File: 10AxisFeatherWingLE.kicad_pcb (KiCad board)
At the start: 2 copper layers, 50.8 x 22.9 mm, 23 parts, among them J1 feather long, J2 feather short, J3 feather long, J4 feather short, J5 feather breakout, J6 stemma connector, U1 LSM9DS1, U2 BMP280

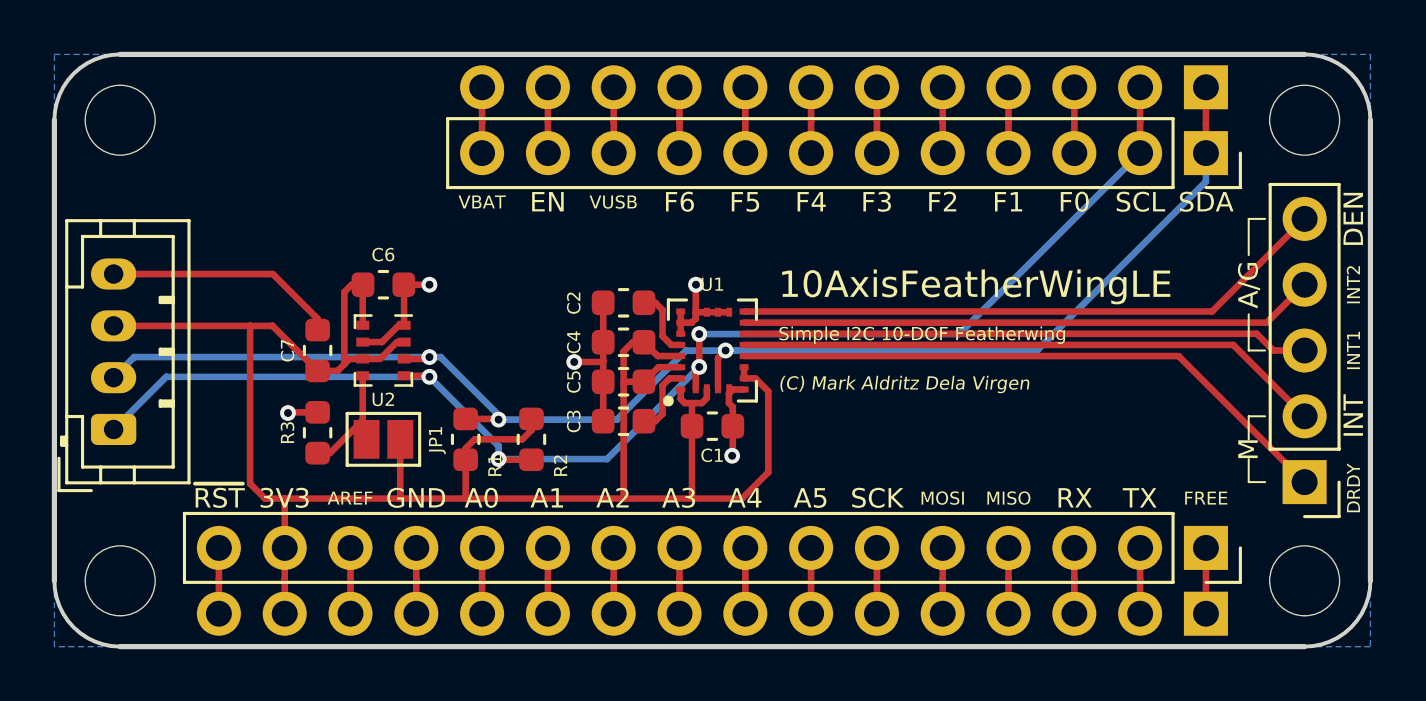
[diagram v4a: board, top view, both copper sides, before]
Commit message: Removed STEMMA connector
STEMMA requires the use of a 3.3V to 5V level shifter and voltage regulator.
The board does not support these features, so they were removed.
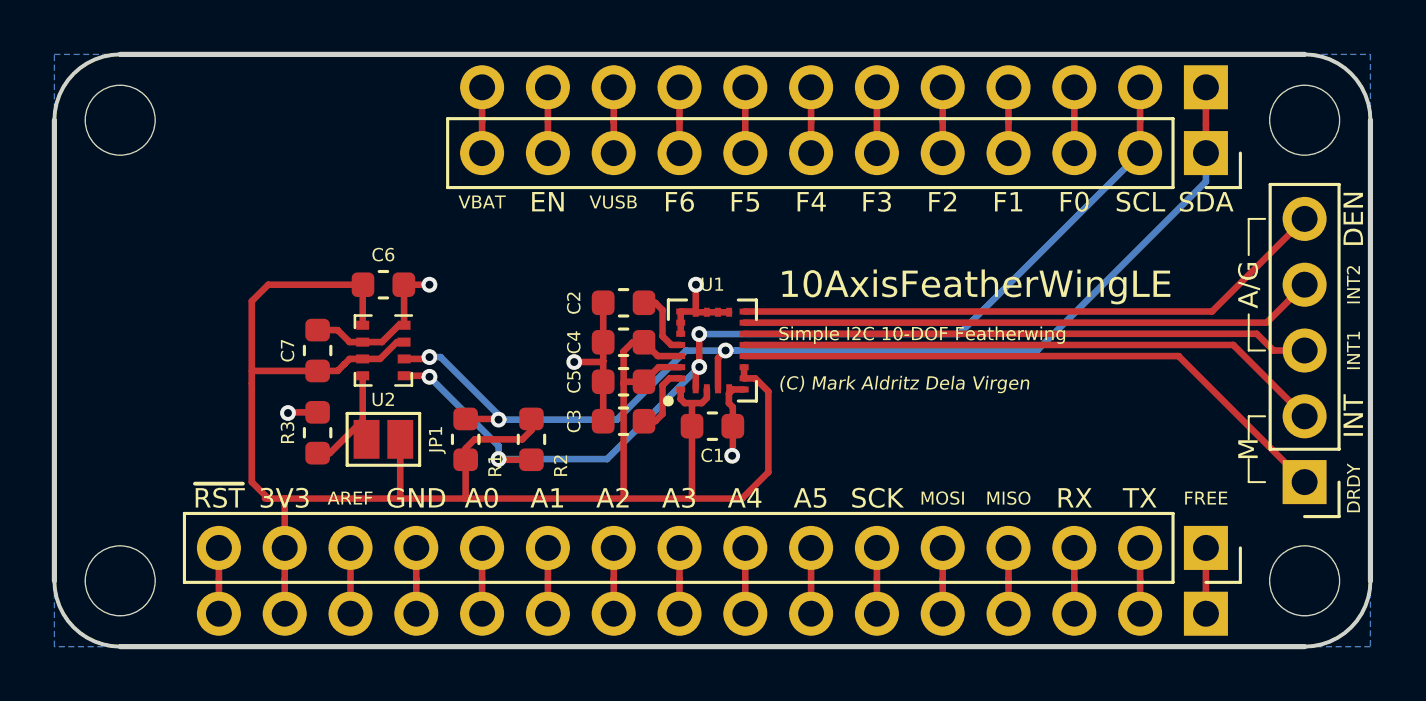
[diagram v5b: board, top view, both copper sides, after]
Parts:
- removed J6: stemma connector, Connector_JST:JST_PH_B4B-PH-K_1x04_P2.00mm_Vertical
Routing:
- net /SCL: track 53.4 -> 40.4 mm
- net /SDA: track 54.9 -> 42.4 mm
- net GND: track 30.1 -> 22.7 mm
- net +3V3: track 77.3 -> 73.1 mm
